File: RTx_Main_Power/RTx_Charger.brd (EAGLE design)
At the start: 15 parts, among them IC1 TL331

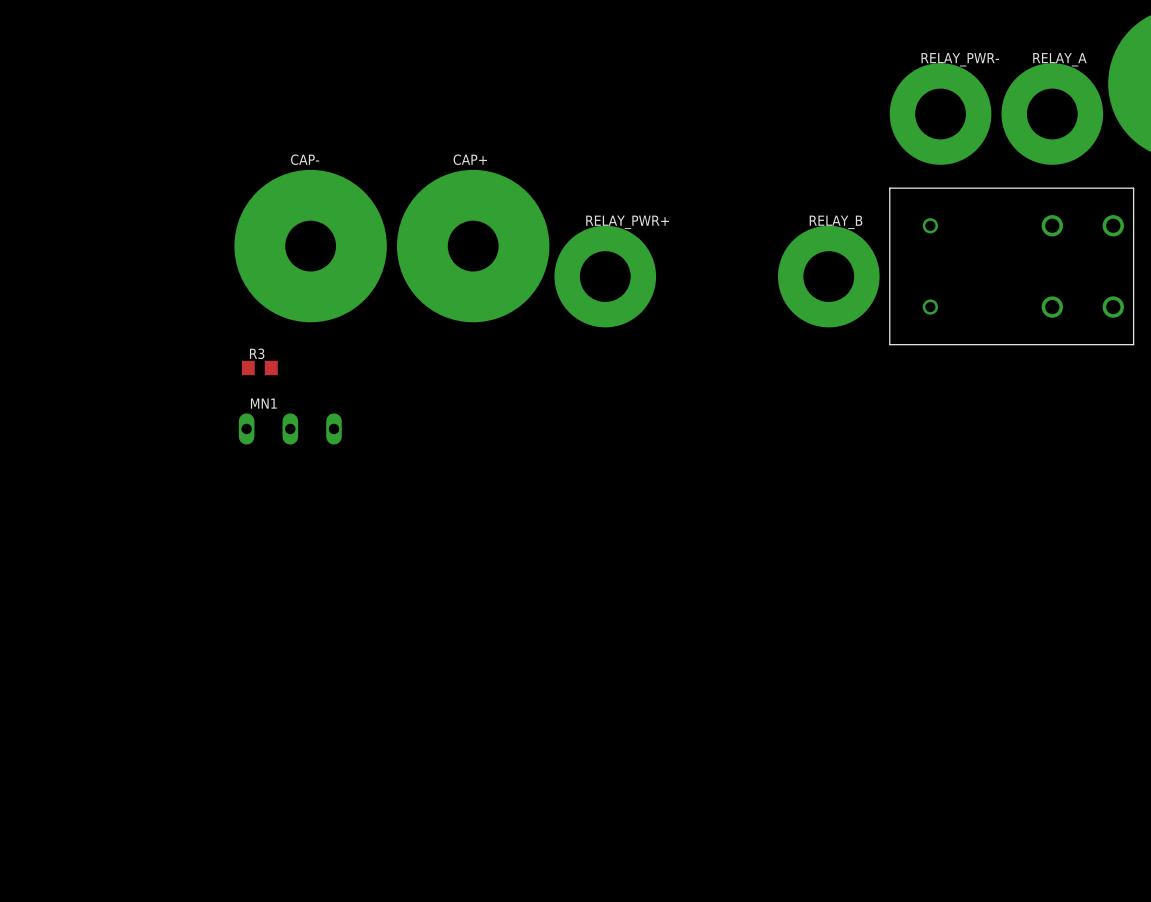
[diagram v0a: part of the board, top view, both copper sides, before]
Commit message: Most recent WPR.docx. Updated charger circuit to reflect potential issue fix.
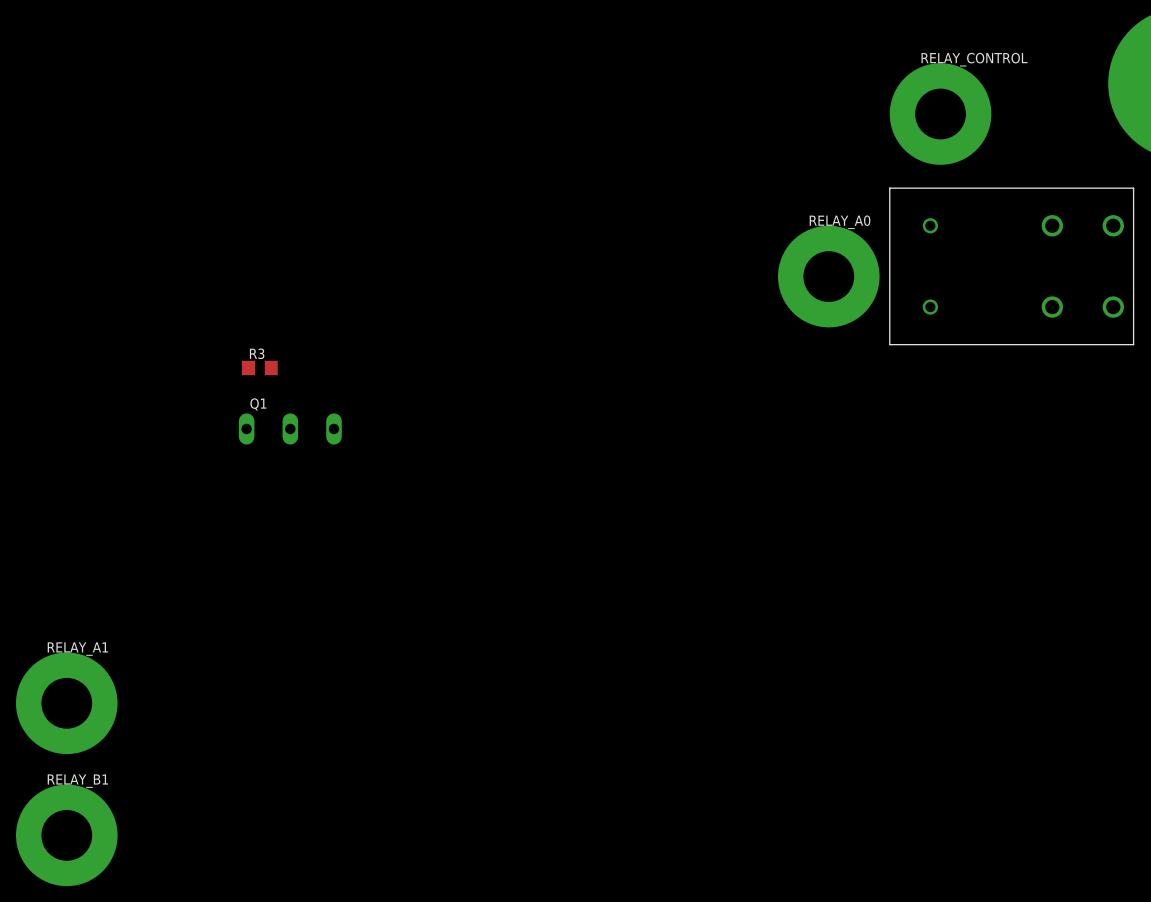
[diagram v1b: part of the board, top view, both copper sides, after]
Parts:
- removed CAP+, CAP-: TERMINAL_CAPACITOR, temp_library:TERMINAL_CAPACITOR
- removed RELAY_A, RELAY_PWR+: TERMINAL_RELAY, temp_library:TERMINAL_RELAY
- added RELAY_A1, RELAY_B1: TERMINAL_RELAY, temp_library:TERMINAL_RELAY
- R3: value o -> 0
- R_CHARGE: value TEH70 -> 10
- renumbered MN1 to Q1, RELAY_B to RELAY_A0, RELAY_PWR- to RELAY_CONTROL, U$2 to RELAY
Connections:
- removed net N$2: RELAY.1, RELAY_CONTROL.P$1
- new net N$7: RELAY.1, RELAY.2, RELAY_CONTROL.P$1
- new net N$8: RELAY.6, RELAY_A1.P$1
- new net N$9: Q1.1, RELAY.4, RELAY_B1.P$1
- net GND: now also RELAY.3; no longer CAP-.P$1, RELAY.4
- net N$3: now also BT+.1; no longer Q1.1, RELAY.2, RELAY.3, RELAY.6
- net N$6: no longer CAP+.P$1
- net VDD: no longer BT+.1, RELAY_A.P$1, RELAY_PWR+.P$1
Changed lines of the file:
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@@
 <element name="R1" library="motorFeedback" package="R1206" value="10k" x="-15.24" y="-52.07"/>
 <element name="R2" library="motorFeedback" package="R1206" value="230k" x="-15.24" y="-57.15"/>
-<element name="R_CHARGE" library="motorFeedback" package="WA-T247-101E" value="TEH70" x="-6.35" y="-78.74"/>
+<element name="R_CHARGE" library="motorFeedback" package="WA-T247-101E" value="10" x="-6.35" y="-78.74"/>
 <element name="BT+" library="temp_library" package="TERMINAL_BATTERY" value="TERMINAL_BATTERY" x="-29.21" y="-78.74"/>
 <element name="BT-" library="temp_library" package="TERMINAL_BATTERY" value="TERMINAL_BATTERY" x="-49.53" y="-78.74"/>
-<element name="RELAY_A" library="temp_library" package="TERMINAL_RELAY" value="TERMINAL_RELAY" x="-66.04" y="-82.55"/>
-<element name="RELAY_PWR-" library="temp_library" package="TERMINAL_RELAY" value="TERMINAL_RELAY" x="-80.01" y="-82.55"/>
-<element name="U$2" library="temp_library" package="G4W-2214P-US-HP" value="G4W-2214P-US-HP" x="-71.12" y="-101.6"/>
-<element name="RELAY_B" library="temp_library" package="TERMINAL_RELAY" value="TERMINAL_RELAY" x="-93.98" y="-102.87"/>
-<element name="RELAY_PWR+" library="temp_library" package="TERMINAL_RELAY" value="TERMINAL_RELAY" x="-121.92" y="-102.87"/>
-<element name="CAP+" library="temp_library" package="TERMINAL_CAPACITOR" value="TERMINAL_CAPACITOR" x="-138.43" y="-99.06"/>
-<element name="CAP-" library="temp_library" package="TERMINAL_CAPACITOR" value="TERMINAL_CAPACITOR" x="-158.75" y="-99.06"/>
-<element name="R3" library="motorFeedback" package="R1206" value="o" x="-165.1" y="-114.3"/>
-<element name="MN1" library="temp_library" package="TO-247" value="STW11NM80" x="-161.29" y="-121.92"/>
+<element name="RELAY_CONTROL" library="temp_library" package="TERMINAL_RELAY" value="TERMINAL_RELAY" x="-80.01" y="-82.55"/>
+<element name="RELAY" library="temp_library" package="G4W-2214P-US-HP" value="G4W-2214P-US-HP" x="-71.12" y="-101.6"/>
+<element name="RELAY_A0" library="temp_library" package="TERMINAL_RELAY" value="TERMINAL_RELAY" x="-93.98" y="-102.87"/>
+<element name="R3" library="motorFeedback" package="R1206" value="0" x="-165.1" y="-114.3"/>
+<element name="Q1" library="temp_library" package="TO-247" value="STW11NM80" x="-161.29" y="-121.92"/>
+<element name="RELAY_A1" library="temp_library" package="TERMINAL_RELAY" value="TERMINAL_RELAY" x="-189.23" y="-156.21"/>
+<element name="RELAY_B1" library="temp_library" package="TERMINAL_RELAY" value="TERMINAL_RELAY" x="-189.23" y="-172.72"/>
 </elements>
 <signals>
@@
 </signal>
 <signal name="VDD">
-<contactref element="BT+" pad="1"/>
 <contactref element="IC1" pad="5"/>
-<contactref element="U$2" pad="5"/>
 <contactref element="R1" pad="2"/>
 <contactref element="R_CHARGE" pad="1"/>
-<contactref element="RELAY_A" pad="P$1"/>
-<contactref element="RELAY_PWR+" pad="P$1"/>
-<wire x1="-81.28" y1="-106.68" x2="-121.92" y2="-102.87" width="0" layer="19" extent="1-1"/>
-<wire x1="-66.04" y1="-82.55" x2="-81.28" y2="-106.68" width="0" layer="19" extent="1-1"/>
-<wire x1="-29.21" y1="-78.74" x2="-66.04" y2="-82.55" width="0" layer="19" extent="1-1"/>
-<wire x1="-11.811" y1="-83.312" x2="-29.21" y2="-78.74" width="0" layer="19" extent="1-1"/>
-<wire x1="-13.818" y1="-52.07" x2="-29.21" y2="-78.74" width="0" layer="19" extent="1-1"/>
+<contactref element="RELAY" pad="5"/>
+<wire x1="-11.811" y1="-83.312" x2="-81.28" y2="-106.68" width="0" layer="19" extent="1-1"/>
+<wire x1="-13.818" y1="-52.07" x2="-11.811" y2="-83.312" width="0" layer="19" extent="1-1"/>
 <wire x1="-16.19" y1="-44.414" x2="-13.818" y2="-52.07" width="0" layer="19" extent="1-1"/>
 </signal>
@@
 <contactref element="BT-" pad="1"/>
 <contactref element="IC1" pad="2"/>
-<contactref element="U$2" pad="4"/>
-<contactref element="CAP-" pad="P$1"/>
-<contactref element="MN1" pad="3"/>
-<wire x1="-49.53" y1="-78.74" x2="-66.04" y2="-96.52" width="0" layer="19" extent="1-1"/>
+<contactref element="Q1" pad="3"/>
+<contactref element="RELAY" pad="3"/>
+<wire x1="-49.53" y1="-78.74" x2="-66.04" y2="-106.68" width="0" layer="19" extent="1-1"/>
 <wire x1="-16.662" y1="-57.15" x2="-49.53" y2="-78.74" width="0" layer="19" extent="1-1"/>
 <wire x1="-15.24" y1="-47.026" x2="-16.662" y2="-57.15" width="0" layer="19" extent="1-1"/>
-<wire x1="-158.75" y1="-99.06" x2="-66.04" y2="-96.52" width="0" layer="19" extent="1-1"/>
-<wire x1="-155.829" y1="-121.92" x2="-158.75" y2="-99.06" width="0" layer="19" extent="1-1"/>
+<wire x1="-155.829" y1="-121.92" x2="-66.04" y2="-106.68" width="0" layer="19" extent="1-1"/>
 </signal>
 <signal name="N$6">
 <contactref element="IC1" pad="3"/>
-<contactref element="CAP+" pad="P$1"/>
 <contactref element="R_CHARGE" pad="3"/>
-<contactref element="RELAY_B" pad="P$1"/>
-<wire x1="-93.98" y1="-102.87" x2="-138.43" y2="-99.06" width="0" layer="19" extent="1-1"/>
+<contactref element="RELAY_A0" pad="P$1"/>
 <wire x1="-0.889" y1="-83.312" x2="-93.98" y2="-102.87" width="0" layer="19" extent="1-1"/>
 <wire x1="-14.29" y1="-47.026" x2="-0.889" y2="-83.312" width="0" layer="19" extent="1-1"/>
-</signal>
-<signal name="N$3">
-<contactref element="U$2" pad="2"/>
-<contactref element="U$2" pad="3"/>
-<contactref element="U$2" pad="6"/>
-<contactref element="MN1" pad="1"/>
-<wire x1="-66.04" y1="-106.68" x2="-81.28" y2="-96.52" width="0" layer="19" extent="1-1"/>
-<wire x1="-58.42" y1="-96.52" x2="-66.04" y2="-106.68" width="0" layer="19" extent="1-1"/>
-<wire x1="-166.751" y1="-121.92" x2="-81.28" y2="-96.52" width="0" layer="19" extent="1-1"/>
-</signal>
-<signal name="N$2">
-<contactref element="U$2" pad="1"/>
-<contactref element="RELAY_PWR-" pad="P$1"/>
-<wire x1="-80.01" y1="-82.55" x2="-58.42" y2="-106.68" width="0" layer="19" extent="1-1"/>
 </signal>
 <signal name="N$1">
@@
 </signal>
 <signal name="N$5">
-<contactref element="MN1" pad="2"/>
+<contactref element="Q1" pad="2"/>
 <contactref element="R3" pad="1"/>
 <wire x1="-166.522" y1="-114.3" x2="-161.29" y2="-121.92" width="0" layer="19" extent="1-1"/>
 </signal>
+<signal name="N$8">
+<contactref element="RELAY_A1" pad="P$1"/>
+<contactref element="RELAY" pad="6"/>
+<wire x1="-189.23" y1="-156.21" x2="-81.28" y2="-96.52" width="0" layer="19" extent="1-1"/>
+</signal>
+<signal name="N$3">
+<contactref element="BT+" pad="1"/>
+</signal>
+<signal name="N$7">
+<contactref element="RELAY" pad="2"/>
+<contactref element="RELAY_CONTROL" pad="P$1"/>
+<contactref element="RELAY" pad="1"/>
+<wire x1="-58.42" y1="-96.52" x2="-58.42" y2="-106.68" width="0" layer="19" extent="1-1"/>
+<wire x1="-80.01" y1="-82.55" x2="-58.42" y2="-96.52" width="0" layer="19" extent="1-1"/>
+</signal>
+<signal name="N$9">
+<contactref element="Q1" pad="1"/>
+<contactref element="RELAY_B1" pad="P$1"/>
+<contactref element="RELAY" pad="4"/>
+<wire x1="-166.751" y1="-121.92" x2="-66.04" y2="-96.52" width="0" layer="19" extent="1-1"/>
+<wire x1="-189.23" y1="-172.72" x2="-166.751" y2="-121.92" width="0" layer="19" extent="1-1"/>
+</signal>
 </signals>

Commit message: Added additional terminals to RTx_Charger board.
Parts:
- removed BT+, BT-: TERMINAL_BATTERY, temp_library:TERMINAL_BATTERY
- removed RELAY_A0, RELAY_A1, RELAY_B1, RELAY_CONTROL: TERMINAL_RELAY, temp_library:TERMINAL_RELAY
- added BAT+_UNSWITCHED: TERMINAL, temp_library:TERMINAL_RELAY
- added BAT_SWITCHED, CAP+, E-STOP_PWR, E-STOP_SWITCHED, GND, HC_RELAY-, RELAY1+, RELAY2-: TERMINAL, temp_library:TERMINAL_BATTERY
- added FUSE: ATO_FUSEHOLDER, temp_library:ATO_BLADE_FUSE
- added HEATSINK: WA-T247-101E, temp_library:WA-T247-101E
- RELAY: value G4W-2214P-US-HP -> G4W-1114P-US-TV8-HP; device temp_library:G4W-2214P-US-HP -> temp_library:G4W-1114P-US-TV8-HP
- R_CHARGE: device motorFeedback:WA-T247-101E -> temp_library:TEH70
- moved R3 251.7 mm to (39.5, 32.3), turned to 90 degrees
- moved Q1 249.5 mm to (39.5, 26.2), turned to 180 degrees
- moved RELAY 210.9 mm to (87.4, 37.6), turned to 180 degrees
- moved R_CHARGE 117.1 mm to (12.4, 36.8), turned to 90 degrees
- moved R2 114.5 mm to (48.0, 38.4)
- moved R1 113.4 mm to (48.0, 42.0)
- moved IC1 102.8 mm to (40.5, 40.6), turned to 180 degrees
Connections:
- removed net N$3: BT+.1
- removed net N$4: IC1.1, R1.1, R2.2
- removed net N$6: IC1.3, RELAY_A0.P$1, R_CHARGE.3
- removed net N$7: RELAY.1, RELAY.2, RELAY_CONTROL.P$1
- removed net N$8: RELAY.6, RELAY_A1.P$1
- removed net N$9: Q1.1, RELAY.4, RELAY_B1.P$1
- removed net VDD: IC1.5, R1.2, RELAY.5, R_CHARGE.1
- new net BAT+_UNSWITCHED: BAT+_UNSWITCHED.P$1, R1.2
- new net BAT_SWITCHED: BAT_SWITCHED.1, FUSE.2.1, FUSE.2.2, FUSE.2.3, FUSE.2.4
- new net CAP+: CAP+.1, IC1.3, R_CHARGE.3
- new net E-STOP_IN: RELAY.5, RELAY1+.1
- new net E-STOP_PWR: E-STOP_PWR.1, FUSE.1.1, FUSE.1.2, FUSE.1.3, FUSE.1.4
- new net E-STOP_SWITCHED: E-STOP_SWITCHED.1, IC1.5, R_CHARGE.1
- new net HC_RELAY-: HC_RELAY-.1, RELAY.1
- new net REFERENCE: IC1.1, R1.1, R2.1
- new net RELAY2-: Q1.1, RELAY2-.1
- net GND: now also GND.1, HEATSINK.HEATSINK1, HEATSINK.HEATSINK2, R2.2, RELAY.4, RELAY.6, R_CHARGE.2; no longer BT-.1, R2.1, RELAY.3
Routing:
- net CAP+: track 0.00 -> 61.5 mm
- net E-STOP_SWITCHED: track 0.00 -> 60.7 mm
- net RELAY2-: track 0.00 -> 25.1 mm
- net REFERENCE: track 0.00 -> 8.84 mm
- net BAT+_UNSWITCHED: track 0.00 -> 7.90 mm
- net N$1: track 0.00 -> 5.68 mm
- net N$5: track 0.00 -> 4.67 mm
- added copper zone on layer 1, net BAT_SWITCHED
- added copper zone on layer 16, net BAT_SWITCHED
- added copper zone on layer 1, net E-STOP_IN
- added copper zone on layer 16, net E-STOP_IN
- added copper zone on layer 1, net E-STOP_PWR
- added copper zone on layer 16, net E-STOP_PWR
- added copper zone on layer 1, net GND
- added copper zone on layer 16, net GND
- added copper zone on layer 1, net HC_RELAY-
- added copper zone on layer 16, net HC_RELAY-
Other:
- board outline added: 102.9 x 75.2 mm
- board text added: "+"
- board text added: "-"
- board text added: "Power Filter Precharge"
- board text added: "RTx"
- board text added: "Robert Corkran Robin Davis Rob Gaskell"

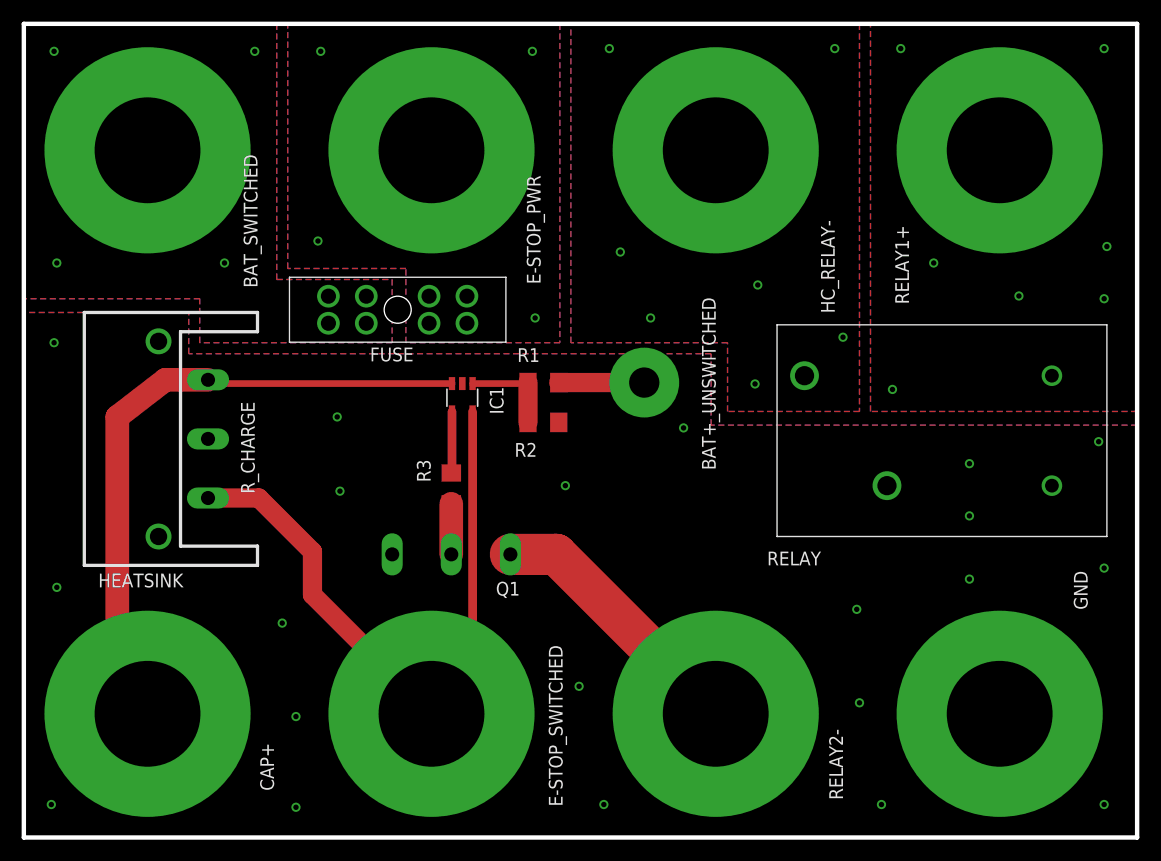
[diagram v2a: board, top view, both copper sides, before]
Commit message: RTx_Charger board layout changed.
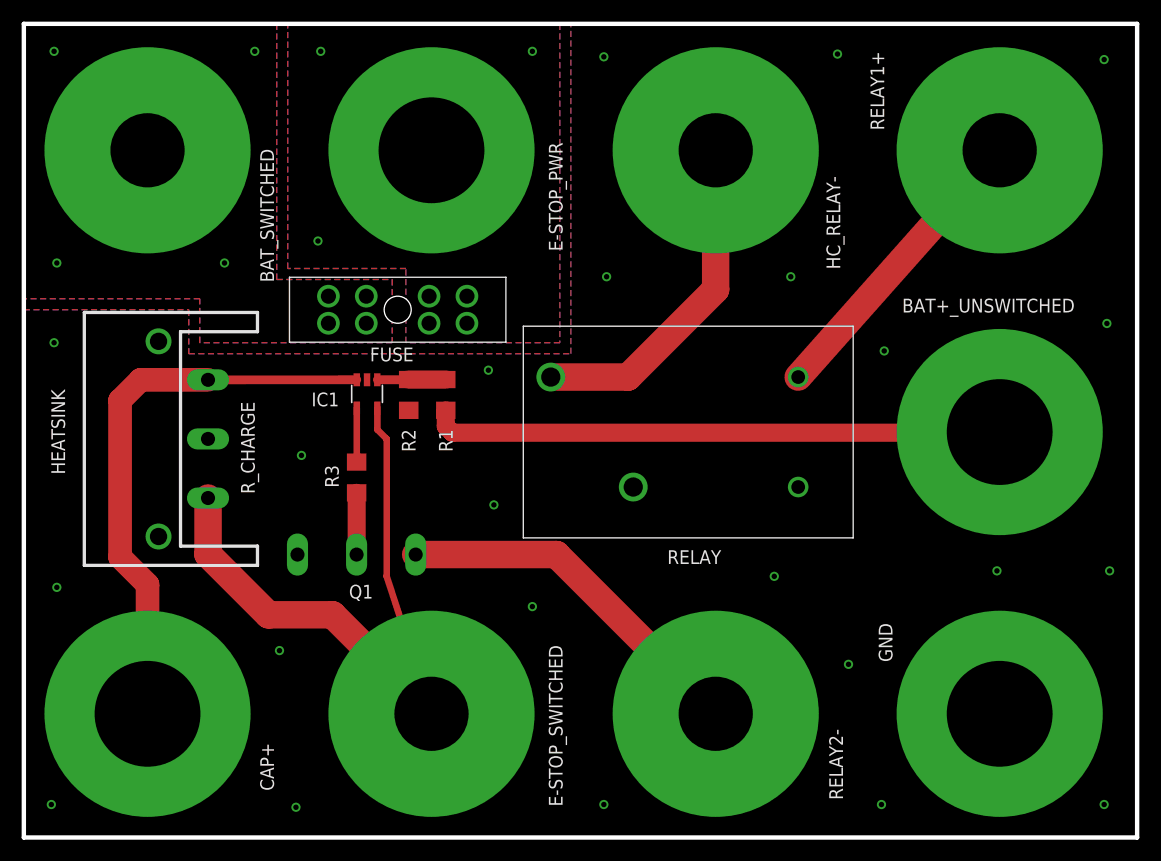
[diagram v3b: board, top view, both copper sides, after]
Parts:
- BAT+_UNSWITCHED: device temp_library:TERMINAL_RELAY -> temp_library:TERMINAL_STUD
- BAT_SWITCHED, E-STOP_SWITCHED, HC_RELAY-, RELAY1+, RELAY2-: device temp_library:TERMINAL_BATTERY -> temp_library:TERMINAL_NO-STUD
- CAP+, E-STOP_PWR, GND: device temp_library:TERMINAL_BATTERY -> temp_library:TERMINAL_STUD
- moved BAT+_UNSWITCHED 33.2 mm to (90.2, 37.5)
- moved RELAY 23.4 mm to (63.9, 37.5)
- moved R2 12.7 mm to (35.6, 40.9), turned to 270 degrees
- moved R1 9.09 mm to (39.0, 40.9), turned to 270 degrees
- moved IC1 8.81 mm to (31.7, 41.0)
- moved R3 8.80 mm to (30.8, 33.3)
- moved Q1 8.75 mm to (30.7, 26.1)
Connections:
- net BAT+_UNSWITCHED: now also BAT+_UNSWITCHED.1; no longer BAT+_UNSWITCHED.P$1
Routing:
- net BAT+_UNSWITCHED: track 7.90 -> 52.9 mm
- net HC_RELAY-: track 0.00 -> 31.4 mm, vias 7 -> 0
- net E-STOP_IN: track 0.00 -> 28.0 mm, vias 7 -> 0
- net CAP+: track 61.5 -> 52.7 mm
- net RELAY2-: track 25.1 -> 33.8 mm
- net REFERENCE: track 8.84 -> 6.35 mm
- net N$5: track 4.67 -> 5.70 mm
- net N$1: track 5.68 -> 5.00 mm
- net E-STOP_SWITCHED: track 60.7 -> 61.2 mm
- removed copper zone on layer 1, net E-STOP_IN
- removed copper zone on layer 16, net E-STOP_IN
- removed copper zone on layer 1, net HC_RELAY-
- removed copper zone on layer 16, net HC_RELAY-
